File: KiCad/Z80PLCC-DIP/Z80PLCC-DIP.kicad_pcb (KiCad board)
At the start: 2 copper layers, 31.8 x 76.2 mm, 8 parts, among them IC1 Z80CPU-LCC, IC2 Z80CPU-DIP

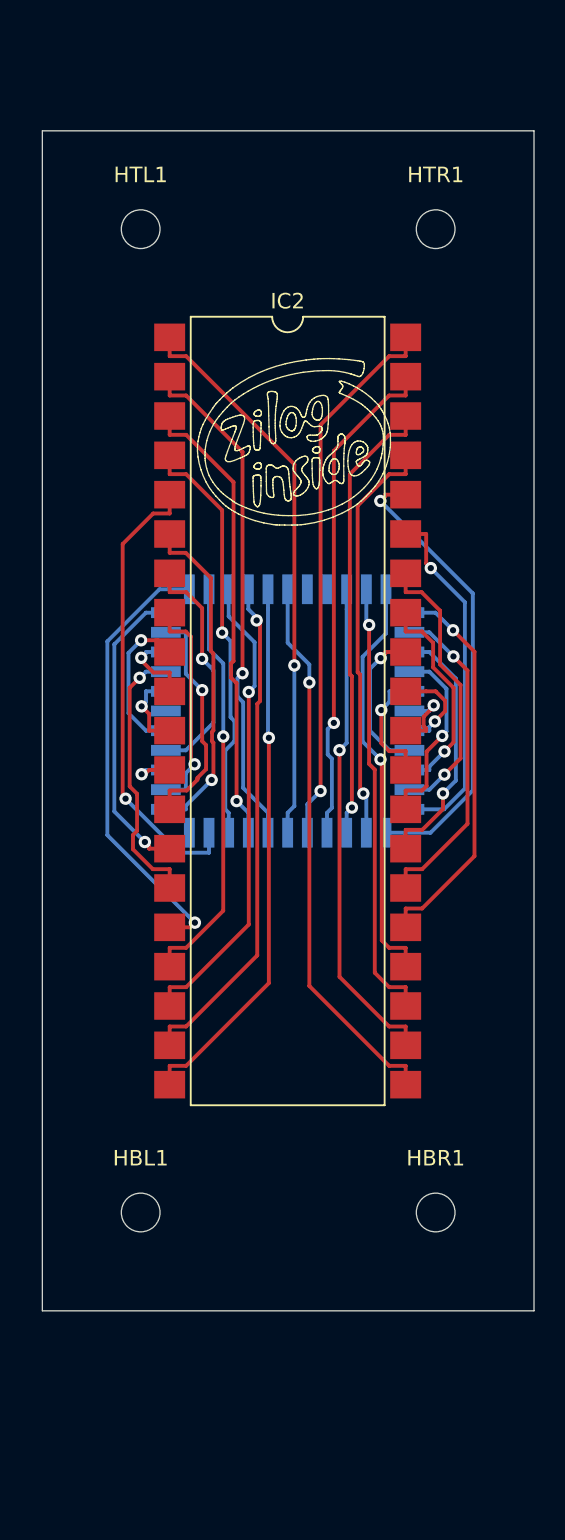
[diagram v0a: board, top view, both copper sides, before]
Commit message: First complete system. Unlikely to work but will serve as the basis of a system to test VGA.
Signed-off-by: John Bradley <flypie@rocketmail.com>
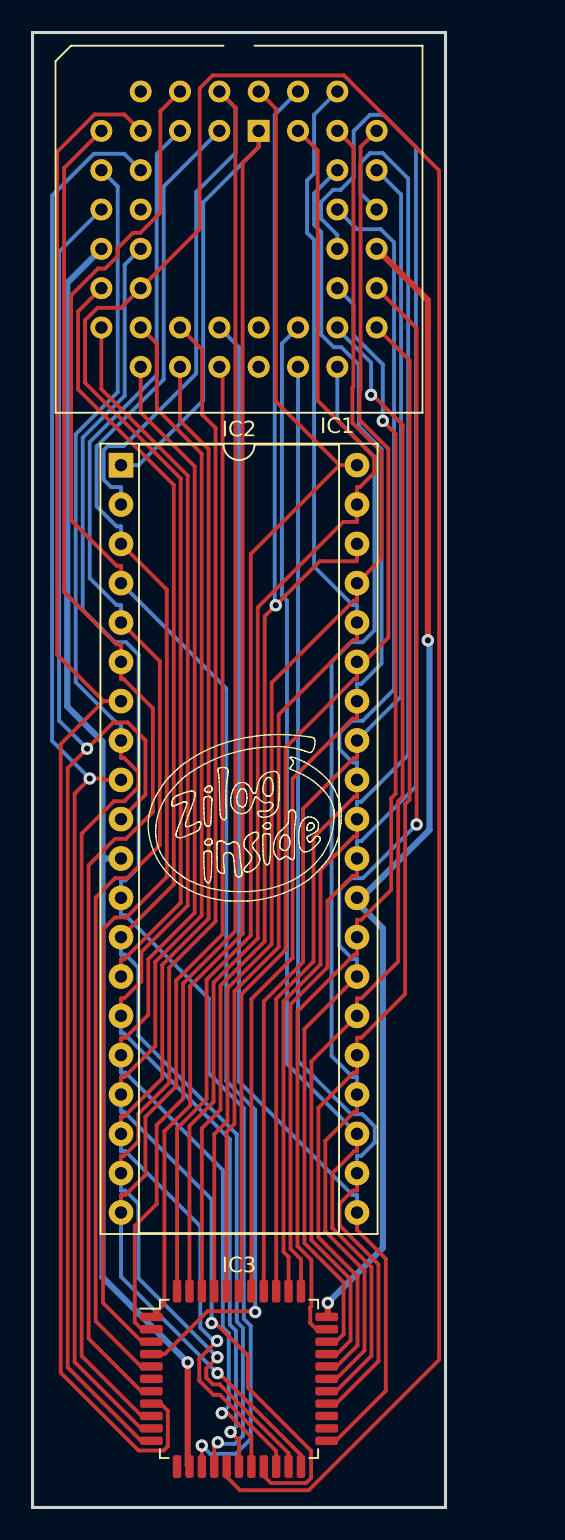
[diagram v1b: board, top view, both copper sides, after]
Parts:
- removed HBL1, HBR1, HTL1, HTR1: MountingHole, MountingHole:MountingHole_2.5mm
- added IC3: Z80CPU-QLP, Package_QFP:LQFP-44_10x10mm_P0.8mm, F.Cu at (127.0, 125.0)
- IC1: footprint Package_LCC:PLCC-44 -> ExtraFootprints:PLCC-44_THT-Socket; moved to F.Cu
- IC2: footprint Package_DIP:SMDIP-40_W15.24mm -> Package_DIP:DIP-40_W15.24mm_Socket
- moved IC1 37.5 mm to (128.3, 44.5)
- moved Logo2 24.5 mm to (120.6, 96.7)
- moved IC2 19.2 mm to (119.4, 66.0)
- moved Logo1 14.2 mm to (119.7, 58.6)
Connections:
- net /~BUSAK renamed /~{BUSAK}
- net /~BUSRQ renamed /~{BUSRQ}
- net /~HALT renamed /~{HALT}
- net /~INT renamed /~{INT}
- net /~IOREQ renamed /~{IOREQ}
- net /~M1 renamed /~{M1}
- net /~MREQ renamed /~{MREQ}
- net /~NMI renamed /~{NMI}
- net /~RD renamed /~{RD}
- net /~REFSH renamed /~{REFSH}
- net /~RESET renamed /~{RESET}
- net /~WAIT renamed /~{WAIT}
- net /~WR renamed /~{WR}
- IC1 pad 10: /DA4 -> /DA5
- IC1 pad 11: /DA5 -> /DA6
- IC1 pad 12: Net-(IC1-Pad12) -> unconnected-(IC1-Pad12)
- IC1 pad 14: /DA1 -> /DA2
- IC1 pad 15: /DA6 -> /DA7
- IC1 pad 16: /DA7 -> /DA0
- IC1 pad 17: /DA0 -> /DA1
- IC1 pad 24: Net-(IC1-Pad24) -> unconnected-(IC1-Pad24)
- IC1 pad 25: Net-(IC1-Pad25) -> unconnected-(IC1-Pad25)
- IC1 pad 6: Net-(IC1-Pad6) -> unconnected-(IC1-Pad6)
- IC1 pad 8: /DA3 -> /DA4
- IC1 pad 9: /DA2 -> /DA3
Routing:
- net /DA0: track 19.6 -> 179.0 mm, vias 1 -> 0
- net /DA6: track 5.33 -> 95.2 mm
- net /A0: track 5.07 -> 92.4 mm, vias 1 -> 0
- net /DA4: track 15.2 -> 101.9 mm, vias 1 -> 0
- net /DA2: track 3.61 -> 89.7 mm
- net /A12: track 33.0 -> 115.9 mm, vias 1 -> 0
- net /DA5: track 10.1 -> 92.8 mm
- net /+5V: track 5.47 -> 84.0 mm
- net /A1: track 6.44 -> 83.1 mm, vias 1 -> 0
- net /DA3: track 14.2 -> 88.1 mm, vias 1 -> 0
- net /DA7: track 14.9 -> 85.7 mm
- net /A11: track 36.1 -> 105.4 mm, vias 1 -> 0
- net /A14: track 27.1 -> 95.2 mm
- net /CLK: track 21.7 -> 89.2 mm, vias 1 -> 0
- net /A2: track 9.88 -> 77.1 mm, vias 1 -> 0
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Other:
- board size 31.8 x 76.2 mm -> 26.7 x 95.2 mm
- net class Default removed
